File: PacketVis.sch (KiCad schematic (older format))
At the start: 36 parts, among them J1 USB_B_Micro, J2 Conn_01x03, SW1 SW_Push_Dual, SW2 SW_SPST, SW3 SW_SPST, U1 3.3V 1A, U2 74HC595, U3 ESP-WROOM-02D

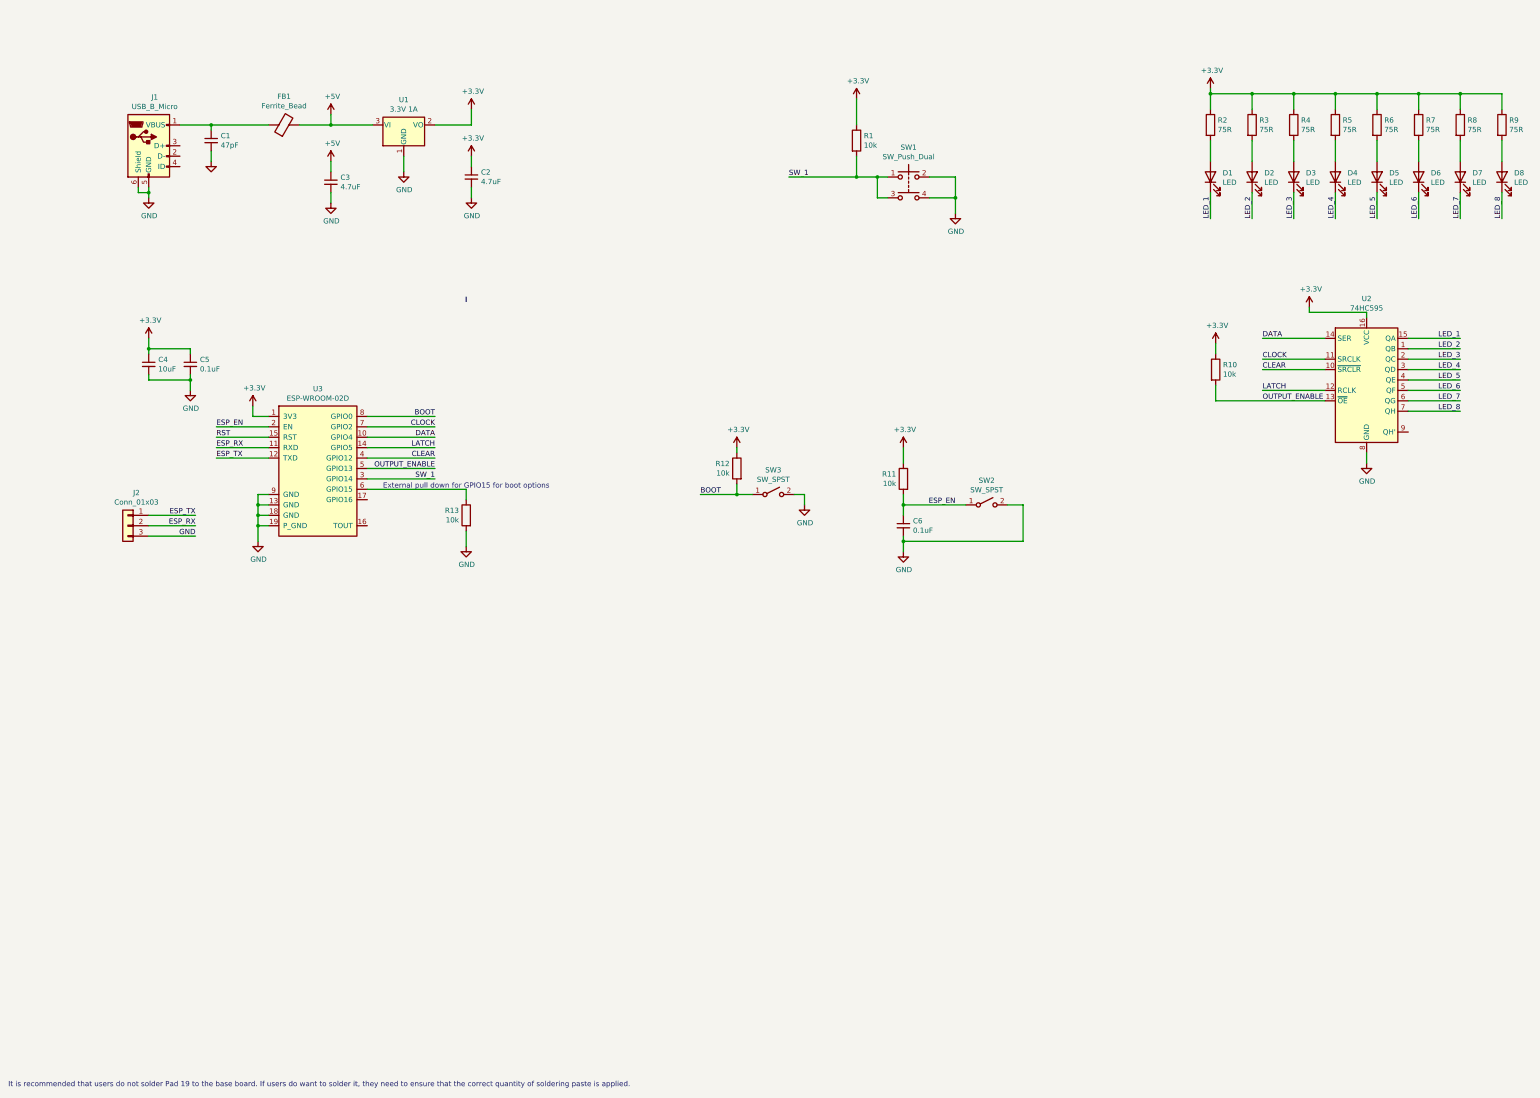
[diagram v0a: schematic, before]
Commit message: Update SCH to A4 page size
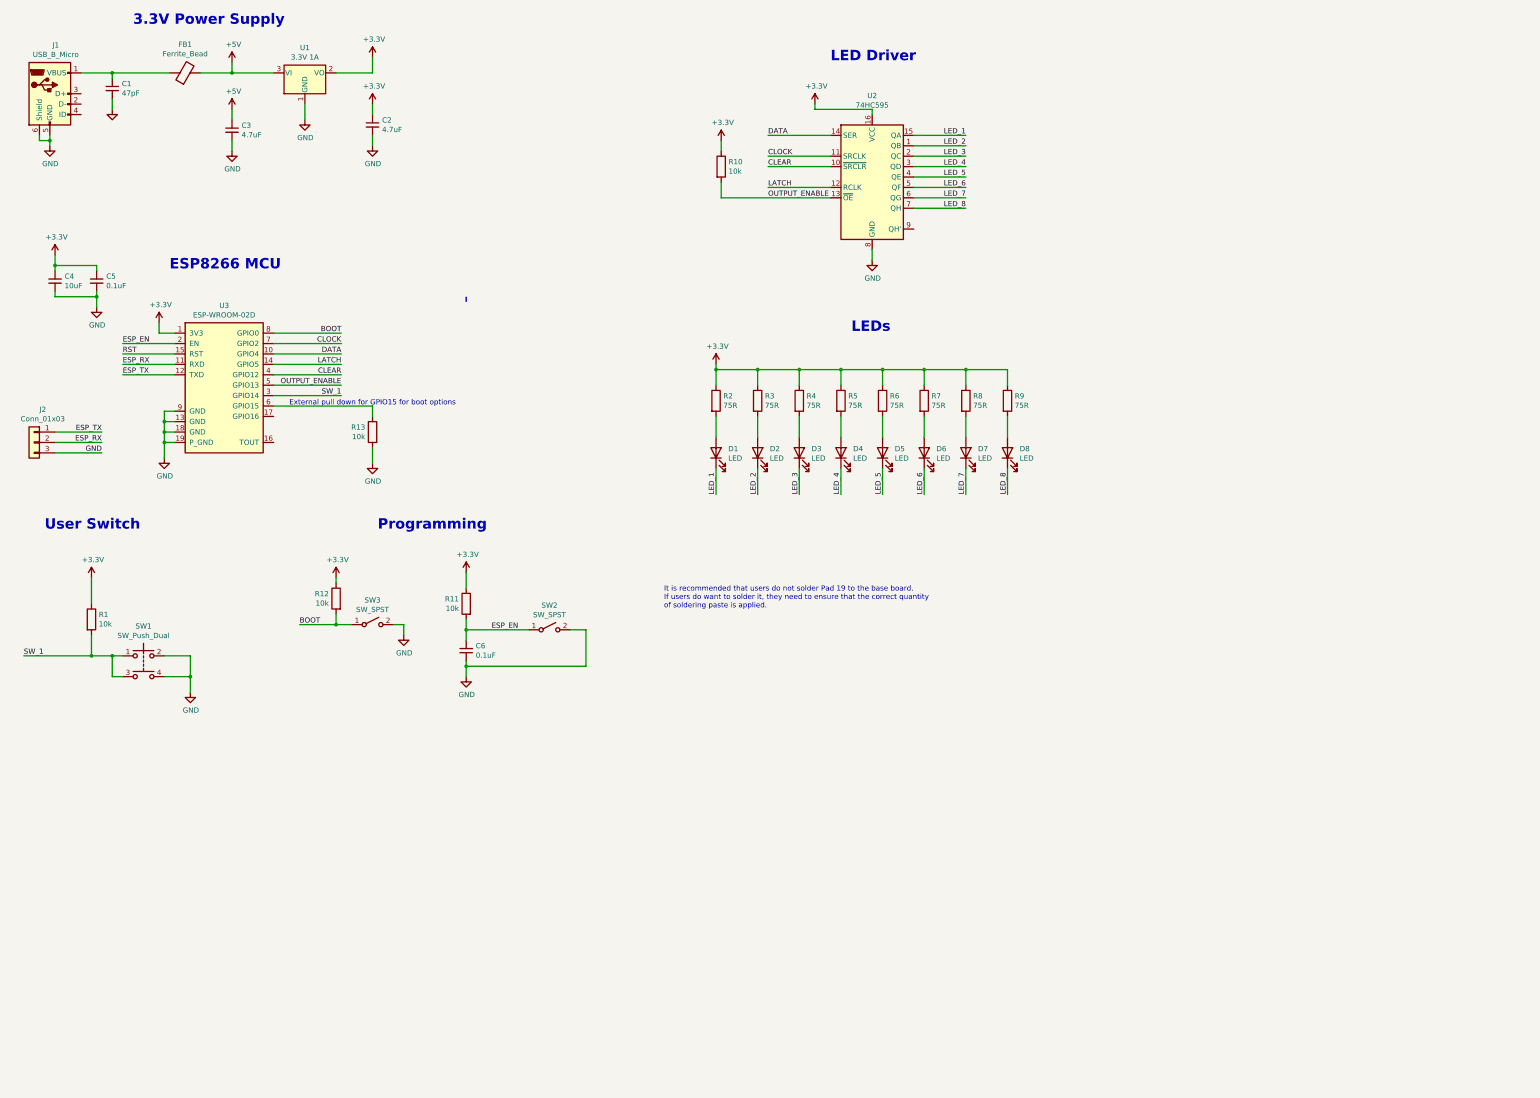
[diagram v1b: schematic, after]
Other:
- note added: "3.3V Power Supply"
- note added: "ESP8266 MCU"
- note added: "It is recommended that users do not solder Pad 19 to the base board. \nIf users do want to solder it, they need to ensure that the correct quantity \nof soldering paste is applied."
- note added: "LED Driver"
- note added: "LEDs"
- note added: "Programming"
- note added: "User Switch\n"
- note removed: "It is recommended that users do not solder Pad 19 to the base board. If users do want to solder it, they need to ensure that the correct quantity of soldering paste is applied."
- moved on the sheet: C1, C2, C3, C4, C5, C6, D1, D2, D3, D4, D5, D6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

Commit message: Add 5V to Programming Header
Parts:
- removed J2: Conn_01x03, Connector_PinHeader_2.54mm:PinHeader_1x03_P2.54mm_Vertical, symbol Connector_Generic:Conn_01x03
- added J2: Conn_01x04, Connector_PinHeader_2.54mm:PinHeader_1x04_P2.54mm_Vertical, symbol Connector_Generic:Conn_01x04
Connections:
- net +5V: now also J2.1 (Pin_1)
- net ESP_RX: now also J2.3 (Pin_3)
- net ESP_TX: now also J2.2 (Pin_2)
- net GND: now also J2.4 (Pin_4)
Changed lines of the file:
@@
 Wire Wire Line
 	1400 1200 1700 1200
-$Comp
-L Connector_Generic:Conn_01x03 J2
-U 1 1 5DEB74FA
-P 950 4750
-F 0 "J2" H 868 5067 50  0000 C CNN
-F 1 "Conn_01x03" H 868 4976 50  0000 C CNN
-F 2 "Connector_PinHeader_2.54mm:PinHeader_1x03_P2.54mm_Vertical" H 950 4750 50  0001 C CNN
-F 3 "~" H 950 4750 50  0001 C CNN
-	1    950  4750
-	-1   0    0    -1
-$EndComp
-Wire Notes Line
-	5100 3400 5100 3350
 Wire Wire Line
 	5100 6900 5100 7000
@@
 Text Notes 8800 3700 0    100  ~ 20
 LEDs
+Wire Notes Line
+	5100 3400 5100 3350
+$Comp
+L Connector_Generic:Conn_01x04 J2
+U 1 1 5E688389
+P 950 4650
+F 0 "J2" H 868 4967 50  0000 C CNN
+F 1 "Conn_01x04" H 868 4876 50  0000 C CNN
+F 2 "Connector_PinHeader_2.54mm:PinHeader_1x04_P2.54mm_Vertical" H 950 4650 50  0001 C CNN
+F 3 "~" H 950 4650 50  0001 C CNN
+	1    950  4650
+	-1   0    0    -1
+$EndComp
+Wire Wire Line
+	1150 4550 1600 4550
+Wire Wire Line
+	1600 4550 1600 4450
+$Comp
+L power:+5V #PWR?
+U 1 1 5E6A2124
+P 1600 4450
+F 0 "#PWR?" H 1600 4300 50  0001 C CNN
+F 1 "+5V" H 1615 4623 50  0000 C CNN
+F 2 "" H 1600 4450 50  0001 C CNN
+F 3 "" H 1600 4450 50  0001 C CNN
+	1    1600 4450
+	1    0    0    -1
+$EndComp
 $EndSCHEMATC

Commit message: Changed U2 to 5v TTL Shift Register needs 5V instead of previous 3.3V Traces rerouted Added PCBA Step File
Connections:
- net +3V3: no longer R10.1, U2.16 (VCC)
- net +5V: now also R10.1, U2.16 (VCC)
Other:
- note added: "External pull down on GPIO15\nfor boot options"
- note removed: "External pull down for GPIO15 for boot options"
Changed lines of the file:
@@
 EESchema Schematic File Version 4
-LIBS:PacketVis-cache
 EELAYER 30 0
 EELAYER END
@@
 Wire Wire Line
 	9400 2500 9900 2500
-$Comp
-L power:+3.3V #PWR011
-U 1 1 5DD1602A
-P 8450 1500
-F 0 "#PWR011" H 8450 1350 50  0001 C CNN
-F 1 "+3.3V" H 8465 1673 50  0000 C CNN
-F 2 "" H 8450 1500 50  0001 C CNN
-F 3 "" H 8450 1500 50  0001 C CNN
-	1    8450 1500
-	1    0    0    -1
-$EndComp
-Wire Wire Line
-	8450 1550 8450 1500
 Text Label 7500 5250 1    50   ~ 0
 LED_1
@@
 	1    0    0    -1
 $EndComp
-$Comp
-L power:+3.3V #PWR013
-U 1 1 5DD54867
-P 7550 1850
-F 0 "#PWR013" H 7550 1700 50  0001 C CNN
-F 1 "+3.3V" H 7565 2023 50  0000 C CNN
-F 2 "" H 7550 1850 50  0001 C CNN
-F 3 "" H 7550 1850 50  0001 C CNN
-	1    7550 1850
-	1    0    0    -1
-$EndComp
 Wire Wire Line
 	7550 1850 7550 1950
@@
 Wire Wire Line
 	4200 4400 4200 4500
-Text Notes 3400 4400 0    50   ~ 0
-External pull down for GPIO15 for boot options
+Text Notes 4300 4700 0    50   ~ 0
+External pull down on GPIO15\nfor boot options
 Wire Wire Line
 	1800 3900 2300 3900
@@
 Wire Wire Line
 	5100 6900 5100 7000
-Wire Wire Line
-	9000 1550 9000 1600
-Wire Wire Line
-	8450 1550 9000 1550
 $Comp
 L 74xx:74HC595 U2
 U 1 1 5DD0EBF3
 P 9000 2200
-F 0 "U2" H 9000 2981 50  0000 C CNN
-F 1 "74HC595" H 9000 2890 50  0000 C CNN
+F 0 "U2" H 9450 3000 50  0000 C CNN
+F 1 "74HC595" H 9450 2900 50  0000 C CNN
 F 2 "PacketVis_Footprints:SOIC-16" H 9000 2200 50  0001 C CNN
 F 3 "http://www.ti.com/lit/ds/symlink/sn74hc595.pdf" H 9000 2200 50  0001 C CNN
@@
 	1    0    0    -1
 $EndComp
+$Comp
+L power:+5V #PWR?
+U 1 1 5F41C719
+P 9000 1500
+F 0 "#PWR?" H 9000 1350 50  0001 C CNN
+F 1 "+5V" H 9015 1673 50  0000 C CNN
+F 2 "" H 9000 1500 50  0001 C CNN
+F 3 "" H 9000 1500 50  0001 C CNN
+	1    9000 1500
+	1    0    0    -1
+$EndComp
+$Comp
+L power:+5V #PWR?
+U 1 1 5F41D0EC
+P 7550 1850
+F 0 "#PWR?" H 7550 1700 50  0001 C CNN
+F 1 "+5V" H 7565 2023 50  0000 C CNN
+F 2 "" H 7550 1850 50  0001 C CNN
+F 3 "" H 7550 1850 50  0001 C CNN
+	1    7550 1850
+	1    0    0    -1
+$EndComp
+Wire Wire Line
+	9000 1500 9000 1600
 $EndSCHEMATC
